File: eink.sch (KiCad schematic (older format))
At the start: 20 parts, among them P301 eInk, Q301 IRLML0030TRPBF

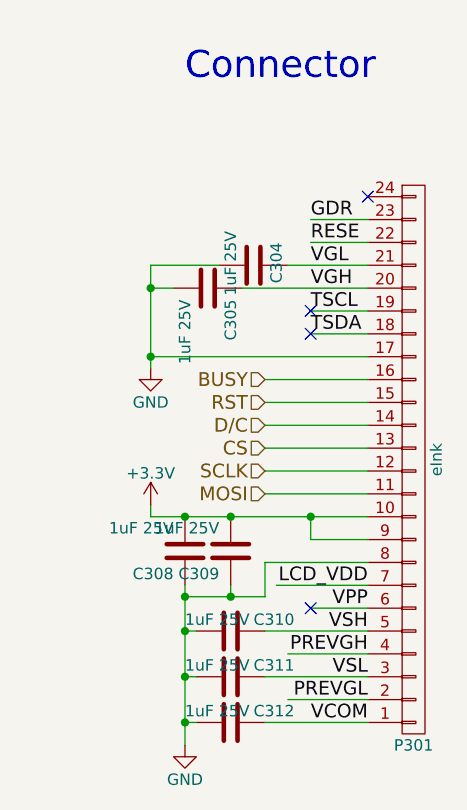
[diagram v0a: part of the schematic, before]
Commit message: Correct e-ink connector direction, reposition & reroute board
Closes #20
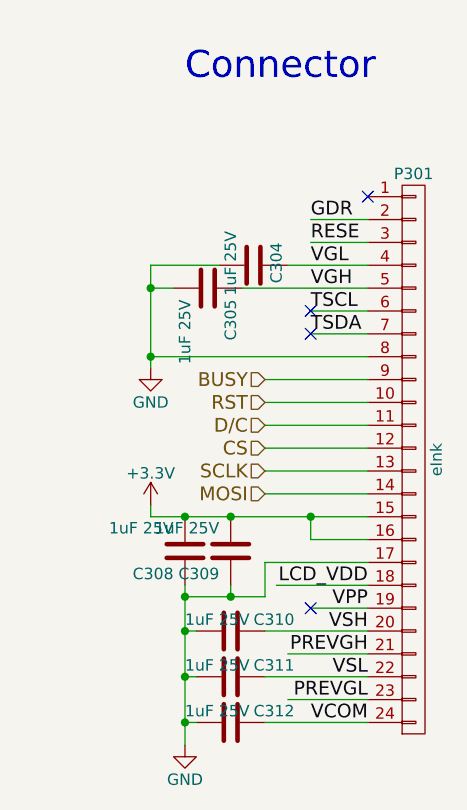
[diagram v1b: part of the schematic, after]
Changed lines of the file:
@@
 F 4 "http://www.szlcsc.com/product/details_11604.html" H 7350 2250 60  0001 C CNN "LCSC"
 	1    7900 4000
-	1    0    0    1
+	1    0    0    -1
 $EndComp
 $Comp

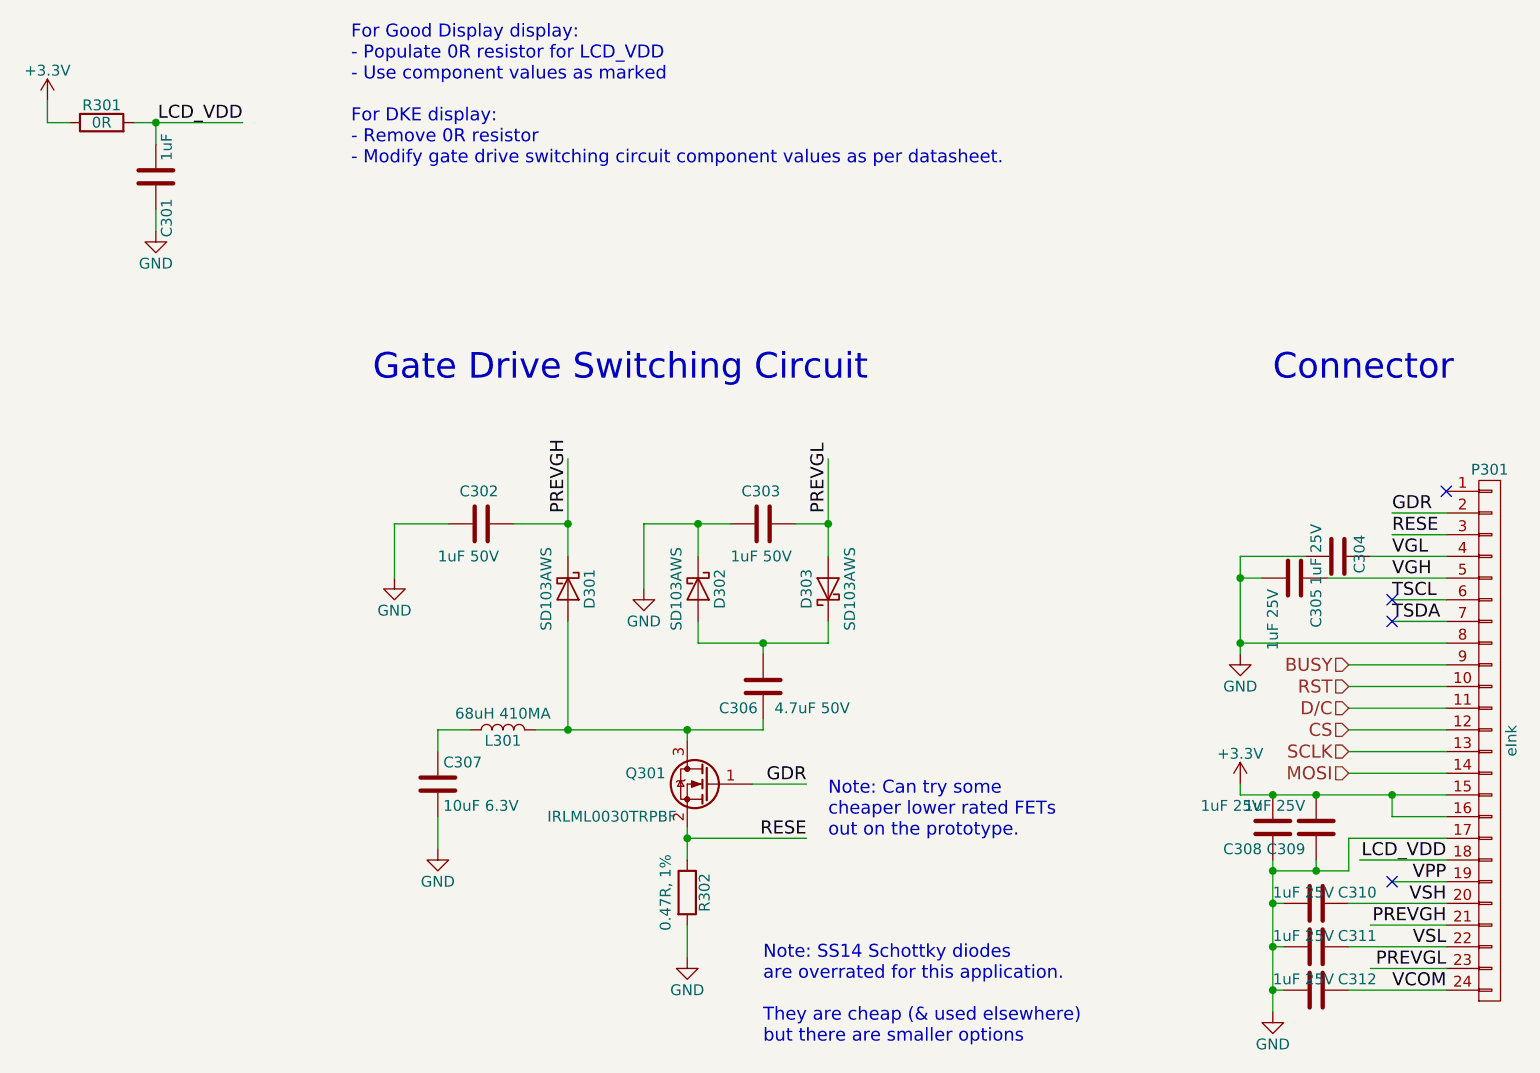
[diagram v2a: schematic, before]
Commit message: Swap to use DEPG0290BNS75AF0-compatible components
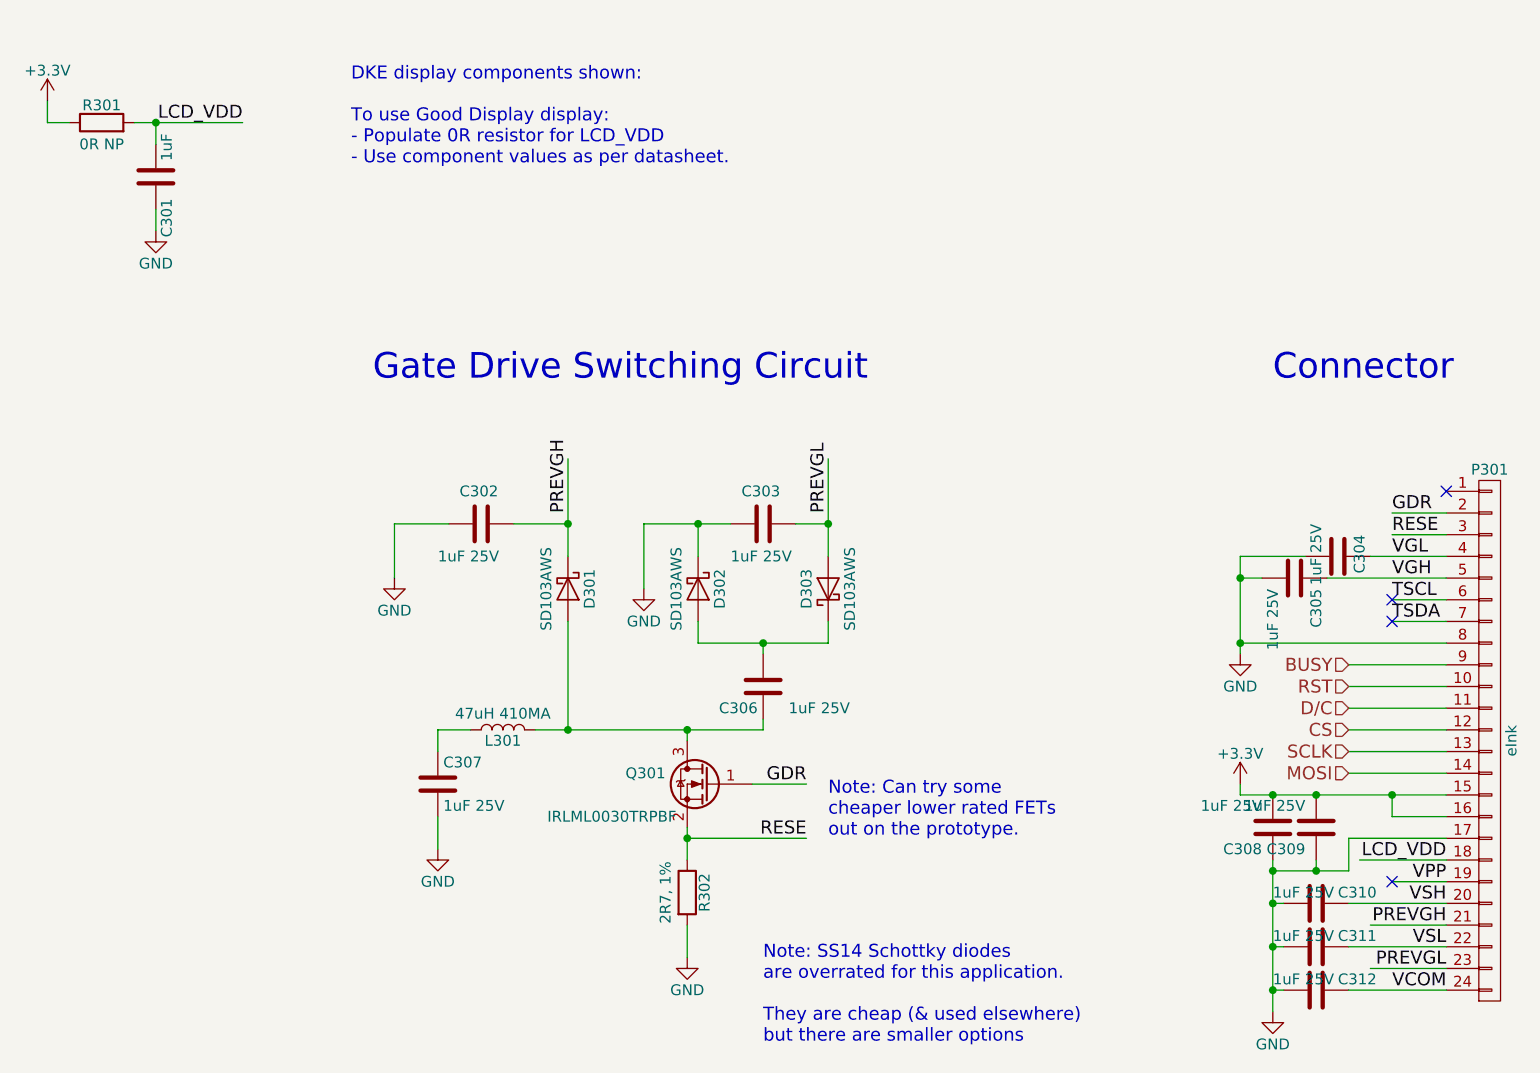
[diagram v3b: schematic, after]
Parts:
- C302, C303: value 1uF 50V -> 1uF 25V
- C306: value 4.7uF 50V -> 1uF 25V; footprint Capacitors_SMD:C_0805_HandSoldering -> Capacitors_SMD:C_0603_HandSoldering
- C307: value 10uF 6.3V -> 1uF 25V; footprint Capacitors_SMD:C_0805_HandSoldering -> Capacitors_SMD:C_0603_HandSoldering
- L301: value 68uH 410MA -> 47uH 410MA; Description FIXED IND 68UH 410MA 1.3 OHM 1210 SMD -> FIXED IND 47UH 410MA 1.3 OHM 1210 SMD; Digikey PN 587-3070-1-ND -> 587-3069-2-ND; LCSC http://www.szlcsc.com/product/details_61593.html -> C113070; MPN CBC3225T680KR -> CBC3225T470KR
- R301: value 0R -> 0R NP
- R302: value 0.47R, 1% -> 2R7, 1%
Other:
- note added: "DKE display components shown:\n\nTo use Good Display display:\n- Populate 0R resistor for LCD_VDD\n- Use component values as per datasheet."
- note removed: "For Good Display display:\n- Populate 0R resistor for LCD_VDD\n- Use component values as marked\n\nFor DKE display:\n- Remove 0R resistor\n- Modify gate drive switching circuit component values as per datasheet."
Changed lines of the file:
@@
 P 1500 1150
 F 0 "R301" V 1580 1150 50  0000 C CNN
-F 1 "0R" V 1500 1150 50  0000 C CNN
+F 1 "0R NP" V 1400 1150 50  0000 C CNN
 F 2 "Resistors_SMD:R_0603_HandSoldering" V 1430 1150 50  0001 C CNN
 F 3 "" H 1500 1150 50  0000 C CNN
@@
 Connection ~ 6900 4250
 Text Notes 2650 1350 0    60   ~ 0
-For Good Display display:\n- Populate 0R resistor for LCD_VDD\n- Use component values as marked\n\nFor DKE display:\n- Remove 0R resistor\n- Modify gate drive switching circuit component values as per datasheet.
+DKE display components shown:\n\nTo use Good Display display:\n- Populate 0R resistor for LCD_VDD\n- Use component values as per datasheet.
 $Comp
 L C C307
@@
 P 3050 4200
 F 0 "C307" H 3075 4300 50  0000 L CNN
-F 1 "10uF 6.3V" H 3075 4100 50  0000 L CNN
-F 2 "Capacitors_SMD:C_0805_HandSoldering" H 3088 4050 50  0001 C CNN
+F 1 "1uF 25V" H 3075 4100 50  0000 L CNN
+F 2 "Capacitors_SMD:C_0603_HandSoldering" H 3088 4050 50  0001 C CNN
 F 3 "" H 3050 4200 50  0001 C CNN
 F 4 "http://www.szlcsc.com/product/details_42881.html" H 7350 2250 60  0001 C CNN "LCSC"
@@
 P 3350 3950
 F 0 "L301" V 3300 3950 50  0000 C CNN
-F 1 "68uH 410MA" V 3425 3950 50  0000 C CNN
+F 1 "47uH 410MA" V 3425 3950 50  0000 C CNN
 F 2 "Capacitors_SMD:C_1210_HandSoldering" H 3350 3950 50  0001 C CNN
 F 3 "" H 3350 3950 50  0001 C CNN
-F 4 "CBC3225T680KR" V 3350 3950 60  0001 C CNN "MPN"
-F 5 "587-3070-1-ND" V 3350 3950 60  0001 C CNN "Digikey PN"
-F 6 "FIXED IND 68UH 410MA 1.3 OHM 1210 SMD" V 3350 3950 60  0001 C CNN "Description"
-F 7 "http://www.szlcsc.com/product/details_61593.html" H 7350 2250 60  0001 C CNN "LCSC"
+F 4 "CBC3225T470KR" V 3350 3950 60  0001 C CNN "MPN"
+F 5 "587-3069-2-ND " V 3350 3950 60  0001 C CNN "Digikey PN"
+F 6 "FIXED IND 47UH 410MA 1.3 OHM 1210 SMD" V 3350 3950 60  0001 C CNN "Description"
+F 7 "C113070" H 7350 2250 60  0001 C CNN "LCSC"
 	1    3350 3950
 	0    -1   -1   0
@@
 P 3250 3000
 F 0 "C302" V 3100 2900 50  0000 L CNN
-F 1 "1uF 50V" V 3400 2800 50  0000 L CNN
+F 1 "1uF 25V" V 3400 2800 50  0000 L CNN
 F 2 "Capacitors_SMD:C_0603_HandSoldering" H 3288 2850 50  0001 C CNN
 F 3 "" H 3250 3000 50  0001 C CNN
@@
 P 4550 3000
 F 0 "C303" V 4400 2900 50  0000 L CNN
-F 1 "1uF 50V" V 4700 2850 50  0000 L CNN
+F 1 "1uF 25V" V 4700 2850 50  0000 L CNN
 F 2 "Capacitors_SMD:C_0603_HandSoldering" H 4588 2850 50  0001 C CNN
 F 3 "" H 4550 3000 50  0001 C CNN
@@
 P 4550 3750
 F 0 "C306" H 4575 3850 50  0000 L CNN
-F 1 "4.7uF 50V" H 4150 3850 50  0000 L CNN
-F 2 "Capacitors_SMD:C_0805_HandSoldering" H 4588 3600 50  0001 C CNN
+F 1 "1uF 25V" H 4150 3850 50  0000 L CNN
+F 2 "Capacitors_SMD:C_0603_HandSoldering" H 4588 3600 50  0001 C CNN
 F 3 "" H 4550 3750 50  0001 C CNN
 F 4 "http://www.szlcsc.com/product/details_107126.html" H 7350 2250 60  0001 C CNN "LCSC"
@@
 P 4200 4700
 F 0 "R302" V 4280 4700 50  0000 C CNN
-F 1 "0.47R, 1%" V 4100 4700 50  0000 C CNN
+F 1 "2R7, 1%" V 4100 4700 50  0000 C CNN
 F 2 "Resistors_SMD:R_0603_HandSoldering" V 4130 4700 50  0001 C CNN
 F 3 "" H 4200 4700 50  0001 C CNN
